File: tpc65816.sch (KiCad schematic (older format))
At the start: 27 parts, among them J1 Barrel_Jack, SW1 RESET, U1 74HC00, U2 74LS245, U3 L7805, U4 WD65C816S, U5 74LS573, U6 IS61C5128AS-25QLI, U7 28C256

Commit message: Edit to main schematic and layout
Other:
- note added: "PRELIMINARY"
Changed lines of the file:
@@
 encoding utf-8
 Sheet 1 3
-Title ""
-Date ""
-Rev ""
+Title "TPC65816 - HalfBurntToast"
+Date "2020-11-19"
+Rev "0.3"
 Comp ""
-Comment1 ""
-Comment2 ""
+Comment1 "PRELIMINARY"
+Comment2 "NOT VERIFIED TO WORK"
 Comment3 ""
 Comment4 ""
@@
 Wire Wire Line
 	1950 1200 1950 1450
+Entry Wire Line
+	3750 4550 3850 4650
+Entry Wire Line
+	3750 4650 3850 4750
+Text GLabel 4100 4650 2    50   Input ~ 0
+A14
+Wire Wire Line
+	3850 4650 4100 4650
+Text Label 3900 4650 0    50   ~ 0
+A14
+Text GLabel 4100 4750 2    50   Input ~ 0
+A15
+Wire Wire Line
+	4100 4750 3850 4750
+Wire Bus Line
+	10950 5150 10950 5450
 Wire Bus Line
 	3750 4350 3750 4800
 Wire Bus Line
-	10950 5150 10950 5450
-Wire Bus Line
 	4150 5550 4150 6250
 Wire Bus Line
@@
 Wire Bus Line
 	5000 2350 5000 4150
+Text Label 3900 4750 0    50   ~ 0
+A15
+Text Notes 7650 2500 0    354  ~ 71
+PRELIMINARY
 $EndSCHEMATC

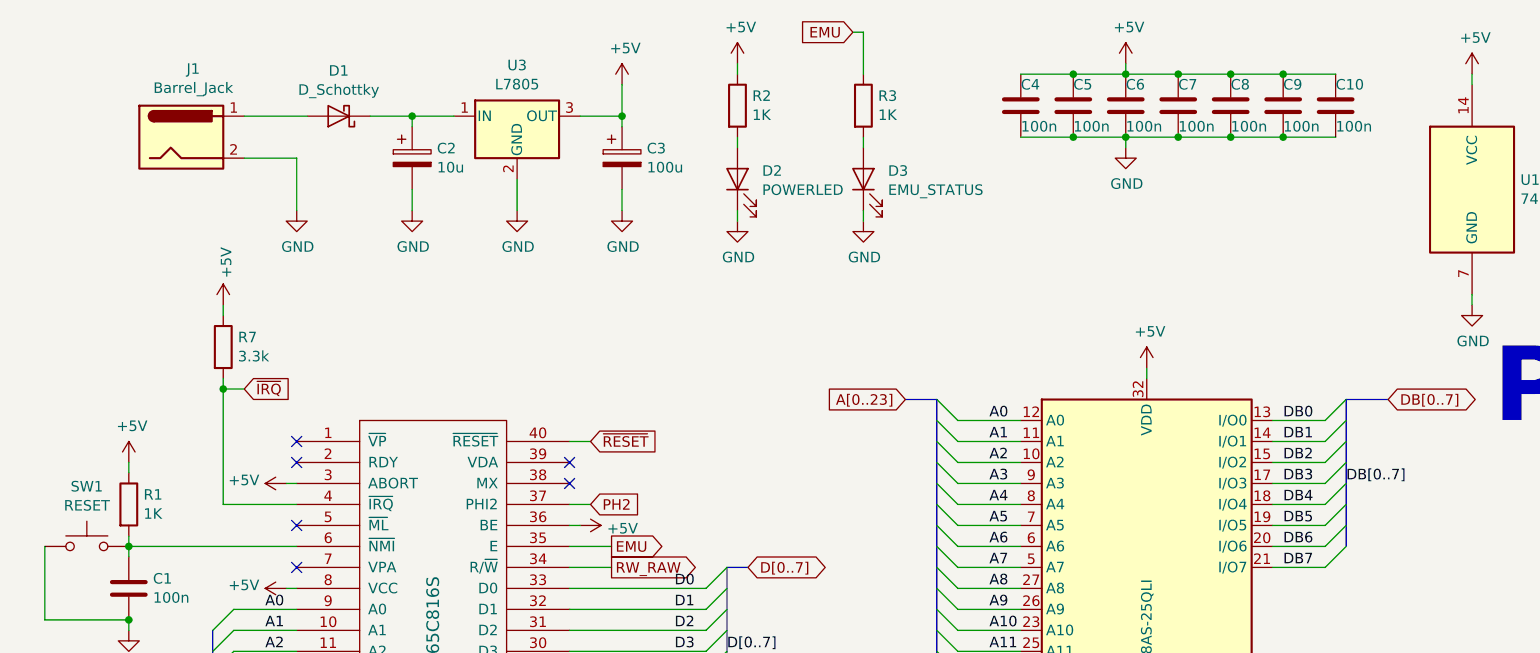
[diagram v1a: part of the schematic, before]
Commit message: Minor cleanup and repositioning - fabricated
Schematic verified. Added power switch. Repositioned PORT A. Cleanup of some traces. Added silkscreen markings. 

Board has been sent to fabrication as of this commit.
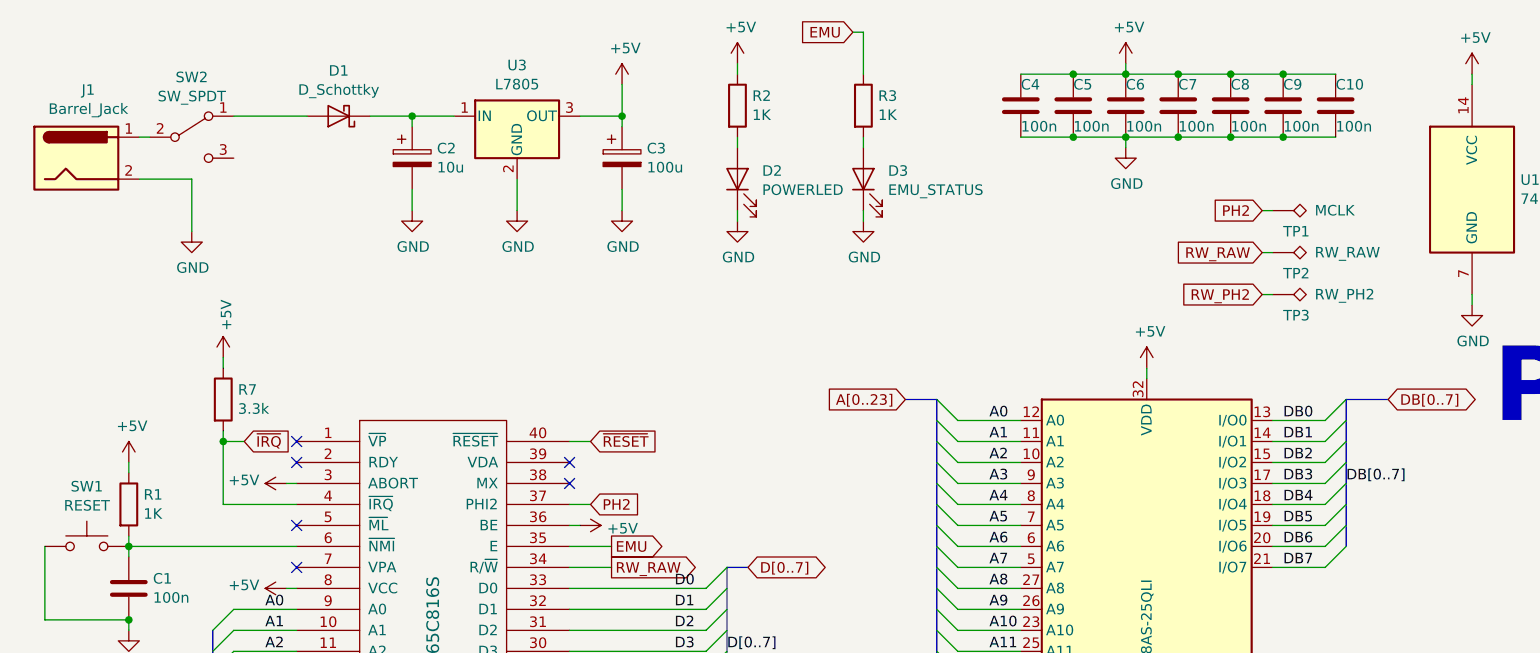
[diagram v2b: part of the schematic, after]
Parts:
- added SW2: SW_SPDT, slide_switch:spdt_slide_switch, symbol Switch:SW_SPDT
- added TP1: MCLK, TestPoint:TestPoint_Pad_1.0x1.0mm, symbol Connector:TestPoint_Alt
- added TP2: RW_RAW, TestPoint:TestPoint_Pad_1.0x1.0mm, symbol Connector:TestPoint_Alt
- added TP3: RW_PH2, TestPoint:TestPoint_Pad_1.0x1.0mm, symbol Connector:TestPoint_Alt
- D2: footprint LED_THT:LED_D3.0mm -> LED_THT:LED_D5.0mm
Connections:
- net PH2: now also TP1.1
- net RW_PH2: now also TP3.1
- net RW_RAW: now also TP2.1
- net at D1.2 (A): now also SW2.1 (A); no longer J1.1
- new net: J1.1, SW2.2 (B)
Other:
- moved on the sheet: J1, R7
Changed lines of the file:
@@
 L Connector:Barrel_Jack J1
 U 1 1 5FB9B723
-P 1400 1100
-F 0 "J1" H 1457 1425 50  0000 C CNN
-F 1 "Barrel_Jack" H 1457 1334 50  0000 C CNN
-F 2 "Connector_BarrelJack:BarrelJack_CUI_PJ-063AH_Horizontal" H 1450 1060 50  0001 C CNN
-F 3 "~" H 1450 1060 50  0001 C CNN
-	1    1400 1100
+P 900 1200
+F 0 "J1" H 957 1525 50  0000 C CNN
+F 1 "Barrel_Jack" H 957 1434 50  0000 C CNN
+F 2 "Connector_BarrelJack:BarrelJack_CUI_PJ-063AH_Horizontal" H 950 1160 50  0001 C CNN
+F 3 "~" H 950 1160 50  0001 C CNN
+	1    900  1200
 	1    0    0    -1
 $EndComp
@@
 L power:GND #PWR03
 U 1 1 5FB9CE9A
-P 1950 1450
-F 0 "#PWR03" H 1950 1200 50  0001 C CNN
-F 1 "GND" H 1955 1277 50  0000 C CNN
-F 2 "" H 1950 1450 50  0001 C CNN
-F 3 "" H 1950 1450 50  0001 C CNN
-	1    1950 1450
+P 1450 1550
+F 0 "#PWR03" H 1450 1300 50  0001 C CNN
+F 1 "GND" H 1455 1377 50  0000 C CNN
+F 2 "" H 1450 1550 50  0001 C CNN
+F 3 "" H 1450 1550 50  0001 C CNN
+	1    1450 1550
 	1    0    0    -1
 $EndComp
@@
 F 0 "D2" V 4089 1183 50  0000 R CNN
 F 1 "POWERLED" V 3998 1183 50  0000 R CNN
-F 2 "LED_THT:LED_D3.0mm" H 4050 1300 50  0001 C CNN
+F 2 "LED_THT:LED_D5.0mm" H 4050 1300 50  0001 C CNN
 F 3 "~" H 4050 1300 50  0001 C CNN
 	1    4050 1300
@@
 NoConn ~ 3250 2650
 NoConn ~ 3250 2750
-Text GLabel 1700 2300 2    50   Input ~ 0
-~IRQ
-$Comp
-L Device:R R7
-U 1 1 6014D281
-P 1600 2100
-F 0 "R7" H 1670 2146 50  0000 L CNN
-F 1 "3.3k" H 1670 2055 50  0000 L CNN
-F 2 "Resistor_THT:R_Axial_DIN0207_L6.3mm_D2.5mm_P7.62mm_Horizontal" V 1530 2100 50  0001 C CNN
-F 3 "~" H 1600 2100 50  0001 C CNN
-	1    1600 2100
-	1    0    0    -1
-$EndComp
 $Comp
 L power:+5V #PWR0103
 U 1 1 6014D7EE
-P 1600 1900
-F 0 "#PWR0103" H 1600 1750 50  0001 C CNN
-F 1 "+5V" V 1615 2028 50  0000 L CNN
-F 2 "" H 1600 1900 50  0001 C CNN
-F 3 "" H 1600 1900 50  0001 C CNN
-	1    1600 1900
-	1    0    0    -1
-$EndComp
-Wire Wire Line
-	1600 1900 1600 1950
-Wire Wire Line
-	1600 2250 1600 2300
-Wire Wire Line
-	1700 2300 1600 2300
+P 1600 2150
+F 0 "#PWR0103" H 1600 2000 50  0001 C CNN
+F 1 "+5V" V 1615 2278 50  0000 L CNN
+F 2 "" H 1600 2150 50  0001 C CNN
+F 3 "" H 1600 2150 50  0001 C CNN
+	1    1600 2150
+	1    0    0    -1
+$EndComp
 Wire Wire Line
 	1950 2850 1600 2850
-Wire Wire Line
-	1600 2850 1600 2300
-Connection ~ 1600 2300
 $Comp
 L power:+5V #PWR0104
@@
 RW_RAW
 Wire Wire Line
-	1700 1000 2000 1000
-Wire Wire Line
-	1700 1200 1950 1200
-Wire Wire Line
-	1950 1200 1950 1450
+	1200 1300 1450 1300
+Wire Wire Line
+	1450 1300 1450 1550
 Entry Wire Line
 	3750 4550 3850 4650
@@
 Wire Wire Line
 	4100 4750 3850 4750
-Wire Bus Line
-	10950 5150 10950 5450
-Wire Bus Line
-	3750 4350 3750 4800
-Wire Bus Line
-	4150 5550 4150 6250
-Wire Bus Line
-	1250 5550 1250 6250
-Wire Bus Line
-	2950 5550 2950 6250
-Wire Bus Line
-	4000 3150 4000 3850
-Wire Bus Line
-	6950 2350 6950 3050
-Wire Bus Line
-	5850 5550 5850 6250
-Wire Bus Line
-	8750 3750 8750 4450
-Wire Bus Line
-	8950 4750 8950 5450
-Wire Bus Line
-	1550 3450 1550 4800
-Wire Bus Line
-	7200 3750 7200 5150
-Wire Bus Line
-	5000 2350 5000 4150
 Text Label 3900 4750 0    50   ~ 0
 A15
 Text Notes 7650 2500 0    354  ~ 71
 PRELIMINARY
+$Comp
+L Connector:TestPoint_Alt TP1
+U 1 1 5FCEFE00
+P 6600 1450
+F 0 "TP1" V 6700 1500 50  0000 L CNN
+F 1 "MCLK" V 6600 1650 50  0000 L CNN
+F 2 "TestPoint:TestPoint_Pad_1.0x1.0mm" H 6800 1450 50  0001 C CNN
+F 3 "~" H 6800 1450 50  0001 C CNN
+	1    6600 1450
+	0    1    1    0
+$EndComp
+$Comp
+L Connector:TestPoint_Alt TP2
+U 1 1 5FD03B0E
+P 6600 1650
+F 0 "TP2" V 6700 1700 50  0000 L CNN
+F 1 "RW_RAW" V 6600 1850 50  0000 L CNN
+F 2 "TestPoint:TestPoint_Pad_1.0x1.0mm" H 6800 1650 50  0001 C CNN
+F 3 "~" H 6800 1650 50  0001 C CNN
+	1    6600 1650
+	0    1    1    0
+$EndComp
+$Comp
+L Connector:TestPoint_Alt TP3
+U 1 1 5FDA9750
+P 6600 1850
+F 0 "TP3" V 6700 1900 50  0000 L CNN
+F 1 "RW_PH2" V 6600 2050 50  0000 L CNN
+F 2 "TestPoint:TestPoint_Pad_1.0x1.0mm" H 6800 1850 50  0001 C CNN
+F 3 "~" H 6800 1850 50  0001 C CNN
+	1    6600 1850
+	0    1    1    0
+$EndComp
+Text GLabel 6550 1450 0    50   Input ~ 0
+PH2
+Wire Wire Line
+	6550 1450 6600 1450
+Text GLabel 6550 1650 0    50   Input ~ 0
+RW_RAW
+Text GLabel 6550 1850 0    50   Input ~ 0
+RW_PH2
+Wire Wire Line
+	6550 1650 6600 1650
+Wire Wire Line
+	6550 1850 6600 1850
+Connection ~ 1600 2550
+Wire Wire Line
+	1700 2550 1600 2550
+Wire Wire Line
+	1600 2500 1600 2550
+Wire Wire Line
+	1600 2150 1600 2200
+$Comp
+L Device:R R7
+U 1 1 6014D281
+P 1600 2350
+F 0 "R7" H 1670 2396 50  0000 L CNN
+F 1 "3.3k" H 1670 2305 50  0000 L CNN
+F 2 "Resistor_THT:R_Axial_DIN0207_L6.3mm_D2.5mm_P7.62mm_Horizontal" V 1530 2350 50  0001 C CNN
+F 3 "~" H 1600 2350 50  0001 C CNN
+	1    1600 2350
+	1    0    0    -1
+$EndComp
+Text GLabel 1700 2550 2    50   Input ~ 0
+~IRQ
+Wire Wire Line
+	1600 2850 1600 2550
+$Comp
+L Switch:SW_SPDT SW2
+U 1 1 5FEC970D
+P 1450 1100
+F 0 "SW2" H 1450 1385 50  0000 C CNN
+F 1 "SW_SPDT" H 1450 1294 50  0000 C CNN
+F 2 "slide_switch:spdt_slide_switch" H 1450 1100 50  0001 C CNN
+F 3 "~" H 1450 1100 50  0001 C CNN
+	1    1450 1100
+	1    0    0    -1
+$EndComp
+Wire Wire Line
+	1650 1000 2000 1000
+Wire Wire Line
+	1200 1100 1250 1100
+Wire Bus Line
+	10950 5150 10950 5450
+Wire Bus Line
+	3750 4350 3750 4800
+Wire Bus Line
+	4150 5550 4150 6250
+Wire Bus Line
+	1250 5550 1250 6250
+Wire Bus Line
+	2950 5550 2950 6250
+Wire Bus Line
+	4000 3150 4000 3850
+Wire Bus Line
+	6950 2350 6950 3050
+Wire Bus Line
+	5850 5550 5850 6250
+Wire Bus Line
+	8750 3750 8750 4450
+Wire Bus Line
+	8950 4750 8950 5450
+Wire Bus Line
+	1550 3450 1550 4800
+Wire Bus Line
+	7200 3750 7200 5150
+Wire Bus Line
+	5000 2350 5000 4150
 $EndSCHEMATC

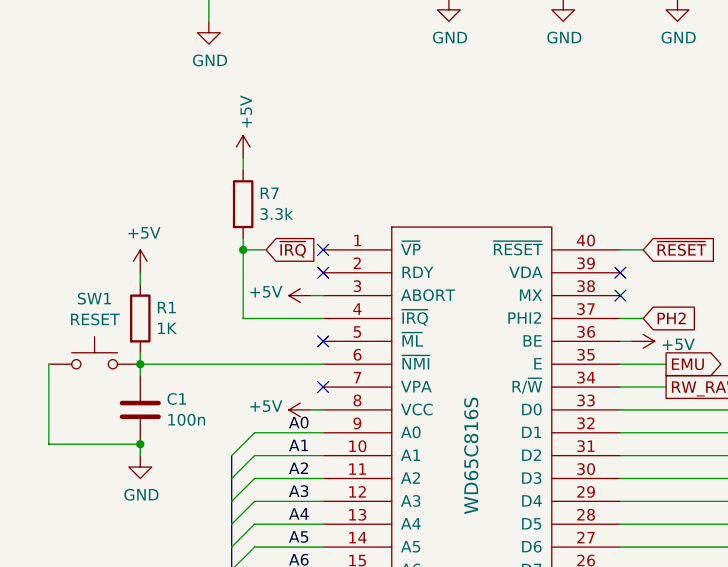
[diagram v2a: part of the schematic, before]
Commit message: Fixed floating rdy pin
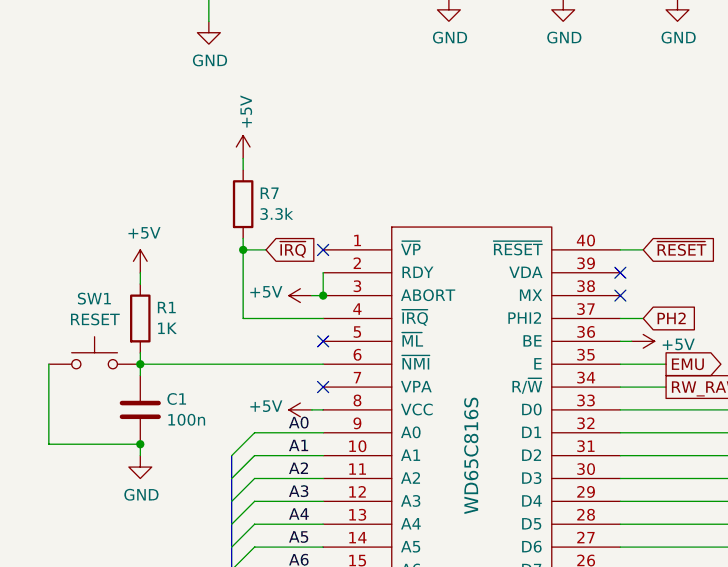
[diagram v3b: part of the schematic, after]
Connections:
- net +5V: now also U4.2 (RDY)
- no-connect marks 19 -> 18
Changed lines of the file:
@@
 Wire Wire Line
 	1900 2750 1950 2750
-NoConn ~ 1950 2650
 Text GLabel 3350 2550 2    50   Input ~ 0
 ~RESET
@@
 Wire Wire Line
 	1200 1100 1250 1100
+Wire Wire Line
+	1950 2650 1950 2750
 Wire Bus Line
 	10950 5150 10950 5450
@@
 Wire Bus Line
 	5000 2350 5000 4150
+Connection ~ 1950 2750
 $EndSCHEMATC

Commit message: Fill update
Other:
- note removed: "PRELIMINARY"
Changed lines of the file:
@@
 Text Label 3900 4750 0    50   ~ 0
 A15
-Text Notes 7650 2500 0    354  ~ 71
-PRELIMINARY
 $Comp
 L Connector:TestPoint_Alt TP1
@@
 Wire Wire Line
 	1950 2650 1950 2750
+Connection ~ 1950 2750
 Wire Bus Line
 	10950 5150 10950 5450
@@
 Wire Bus Line
 	5000 2350 5000 4150
-Connection ~ 1950 2750
 $EndSCHEMATC

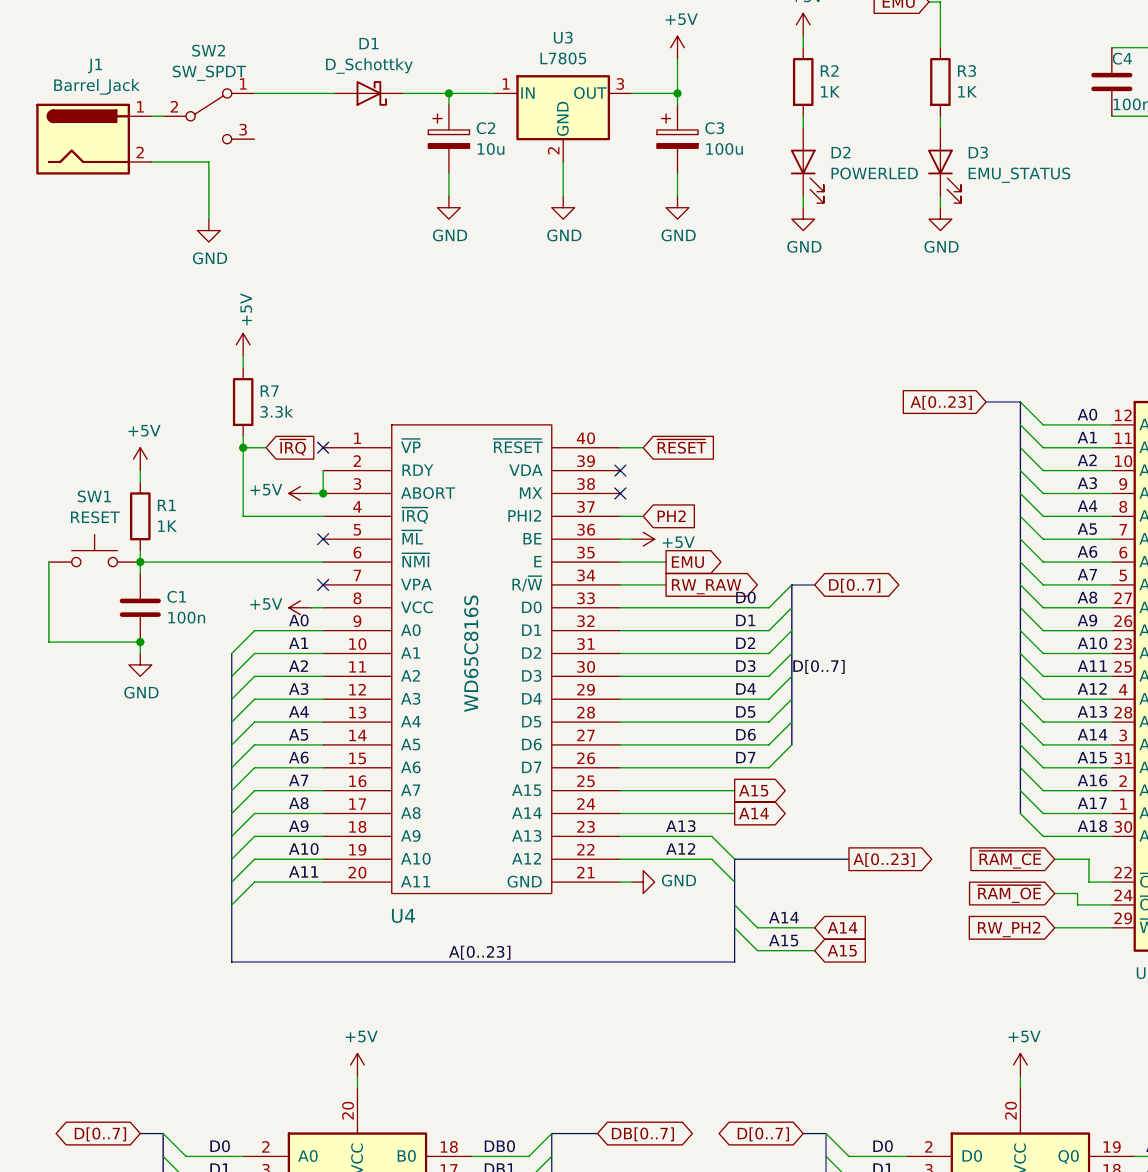
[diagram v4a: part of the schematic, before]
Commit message: Fix to RDY pin
RDY needs to be pulled up with a resistor and not linked to VDD directly. Unlike the 65c02, RDY on the 65c816 is bidirectional and can, under some circumstances, attempt to pull itself down. If it's directly connected to VDD, it will attempt to sink VDD and short out. WDC seems to recommend using 3.3K resistors as pullups. I'm not sure how other values would perform. BE is now pulled up with a resistor too, which is recommended by WDC for reasons I'm not sure about.
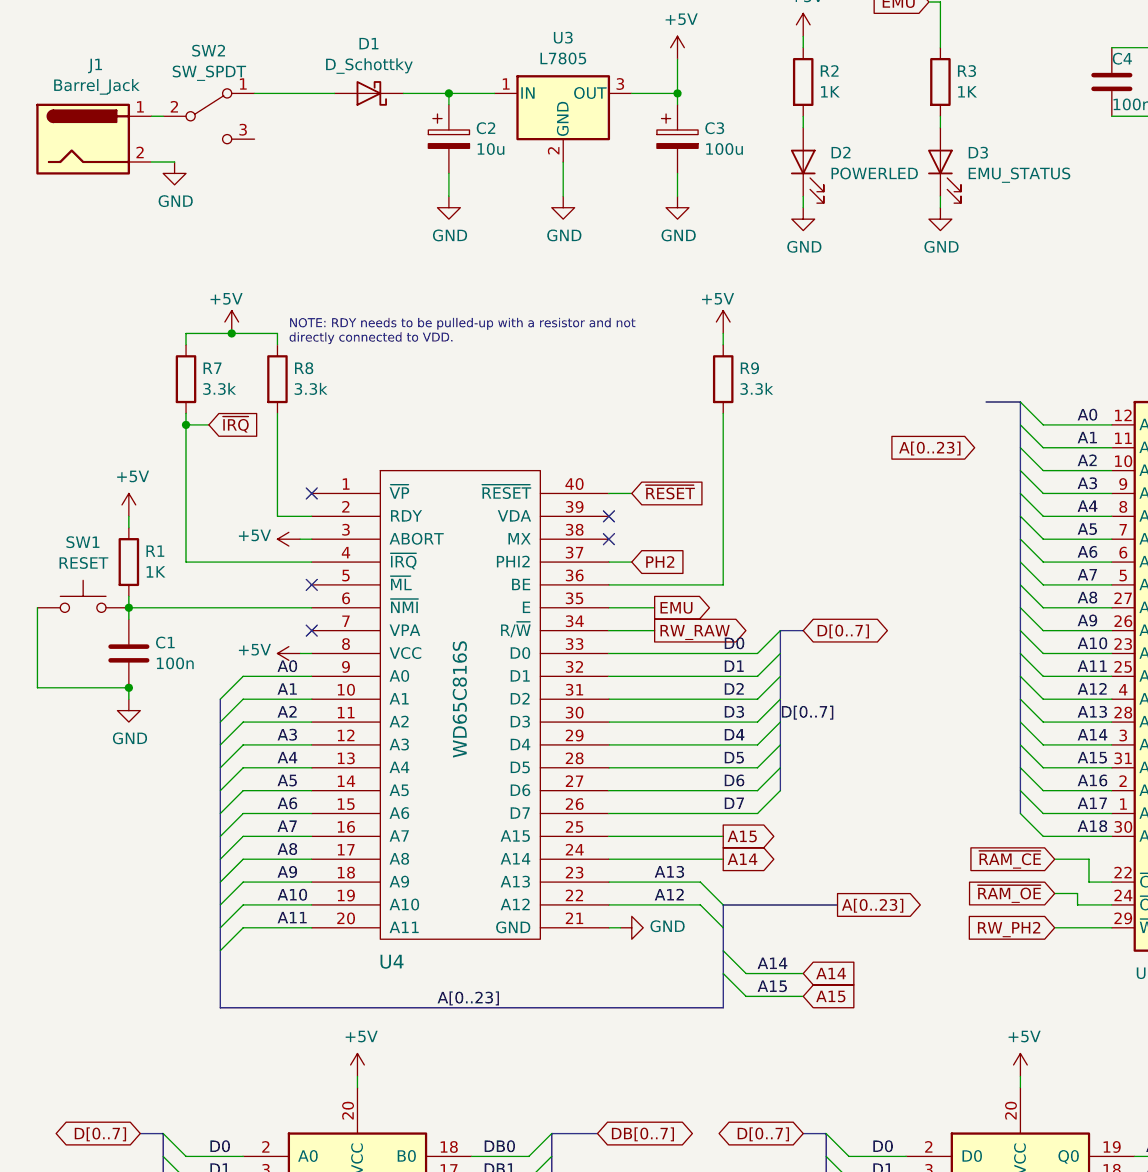
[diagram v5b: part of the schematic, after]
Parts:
- added R8, R9: 3.3k, Resistor_SMD:R_1206_3216Metric_Pad1.42x1.75mm_HandSolder, symbol Device:R
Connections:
- net +5V: now also R8.1, R9.1; no longer U4.2 (RDY), U4.36 (BE)
- new net: R8.2, U4.2 (RDY)
- new net: R9.2, U4.36 (BE)
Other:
- note added: "NOTE: RDY needs to be pulled-up with a resistor and not \ndirectly connected to VDD."
- moved on the sheet: C1, R1, R7, SW1, U4

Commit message: MAJOR FIXES - UNTESTED
Fixes for voltage regulator and barrel jack footprint. Fix for 245 direction. Fix for 65C22 PLCC pin layout. Complete rerouting of board.
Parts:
- J1: footprint Connector_BarrelJack:BarrelJack_CUI_PJ-063AH_Horizontal -> Connector_BarrelJack:BarrelJack_Horizontal
- U3: renamed from U4; symbol 6502:WD65C816S -> tpc65816-rescue:WD65C816S-6502
- U4: renamed from U3; footprint Package_TO_SOT_THT:TO-126-3_Horizontal_TabDown -> Package_TO_SOT_THT:TO-220-3_Horizontal_TabDown
- renumbered R7 to R2, R8 to R3, R9 to R4, R2 to R5, R3 to R6
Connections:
- net D0: now also U2.18 (B0); no longer U2.2 (A0)
- net D1: now also U2.17 (B1); no longer U2.3 (A1)
- net D2: now also U2.16 (B2); no longer U2.4 (A2)
- net D3: now also U2.15 (B3); no longer U2.5 (A3)
- net D4: now also U2.14 (B4); no longer U2.6 (A4)
- net D5: now also U2.13 (B5); no longer U2.7 (A5)
- net D6: now also U2.12 (B6); no longer U2.8 (A6)
- net D7: now also U2.11 (B7); no longer U2.9 (A7)
- net DB0: now also U2.2 (A0); no longer U2.18 (B0)
- net DB1: now also U2.3 (A1); no longer U2.17 (B1)
- net DB2: now also U2.4 (A2); no longer U2.16 (B2)
- net DB3: now also U2.5 (A3); no longer U2.15 (B3)
- net DB4: now also U2.6 (A4); no longer U2.14 (B4)
- net DB5: now also U2.7 (A5); no longer U2.13 (B5)
- net DB6: now also U2.8 (A6); no longer U2.12 (B6)
- net DB7: now also U2.9 (A7); no longer U2.11 (B7)
- net RW_RAW: now also U2.19 (CE); no longer U2.1 (A->B)
- net at U1.11, U5.11 (Load): now also U2.1 (A->B); no longer U2.19 (CE)
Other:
- moved on the sheet: U1D
